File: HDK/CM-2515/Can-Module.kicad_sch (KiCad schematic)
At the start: 13 parts, among them J101 Can Connect, J102 Can Connect, SW101 SW_DIP_x01, U101 SN65HVD230, U102 MCP2515-xST, Y101 8MHz

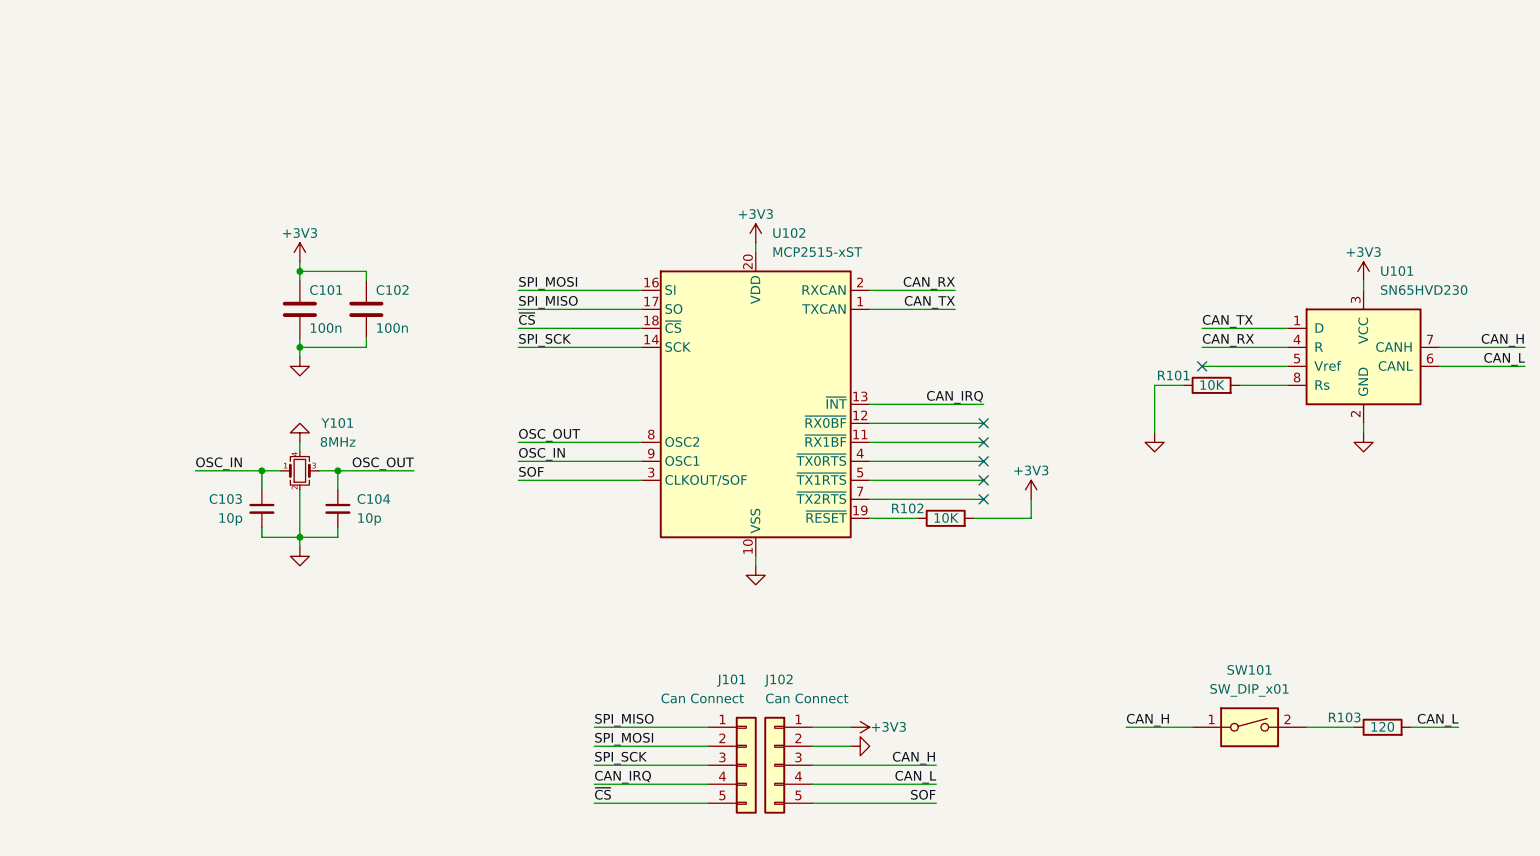
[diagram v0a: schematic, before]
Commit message: updated CM2515
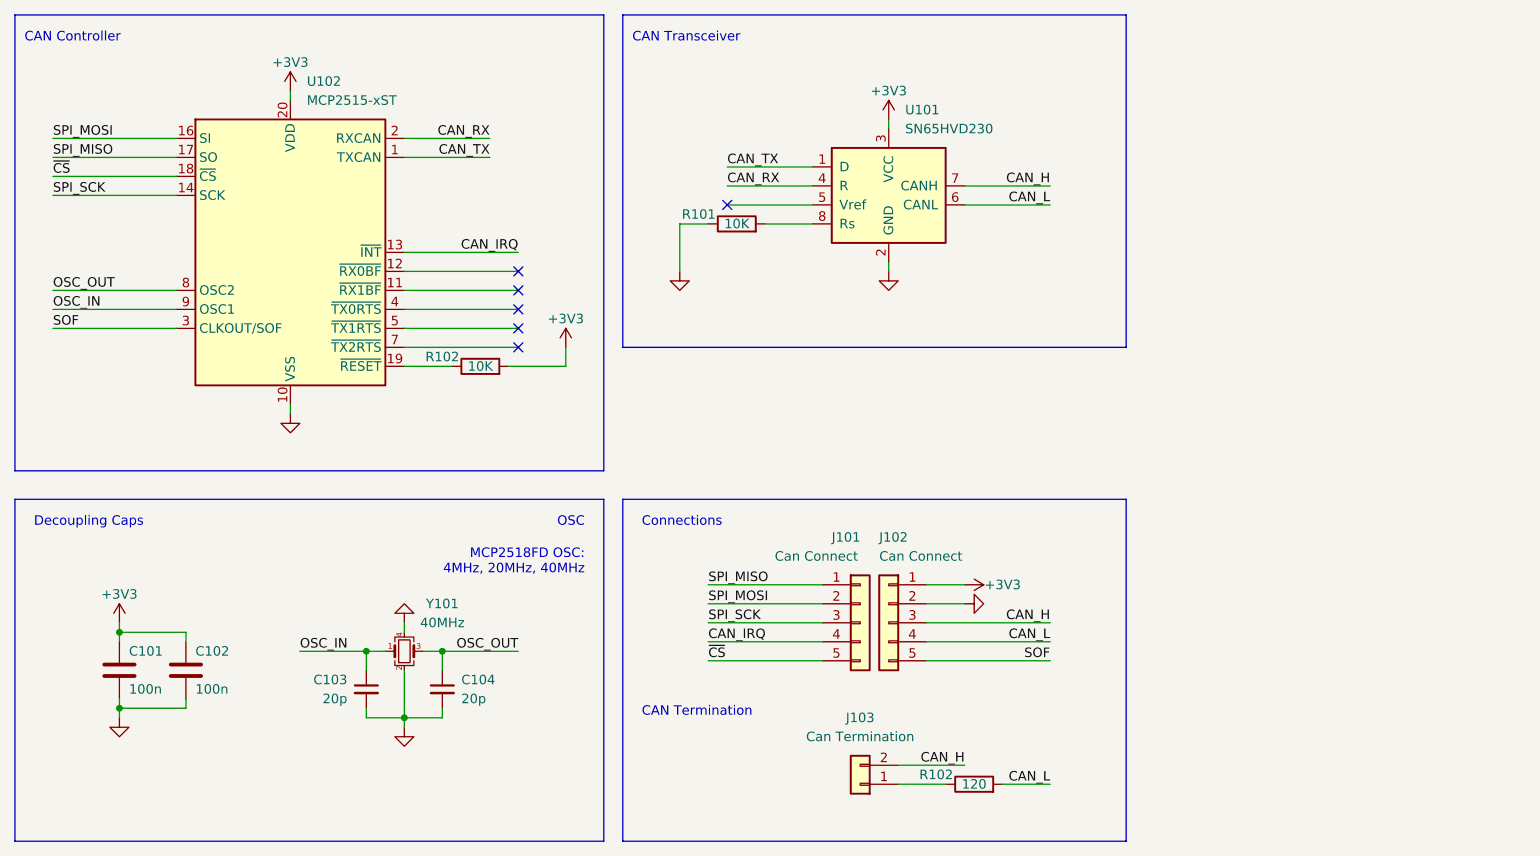
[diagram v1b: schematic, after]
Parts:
- removed R102: 10K, Resistor_SMD:R_0402_1005Metric, symbol Device:R
- removed R103: 120, Resistor_SMD:R_0402_1005Metric, symbol Device:R
- removed SW101: SW_DIP_x01, Button_Switch_SMD:SW_DIP_SPSTx01_Slide_9.78x4.72mm_W8.61mm_P2.54mm, symbol Switch:SW_DIP_x01
- added J103: Can Termination, NVF-Kicad:PinHeader_1x02_P2.54mm_Horizontal, symbol Connector_Generic:Conn_01x02
- added R102: 120, Resistor_SMD:R_0805_2012Metric, symbol Device:R
- added R102: 10K, Resistor_SMD:R_0402_1005Metric, symbol Device:R
- C101, C102: LCSC (none) -> C1523
- C103, C104: value 10p -> 20p; LCSC (none) -> C1554
- R101: LCSC (none) -> C25744
- U101: LCSC (none) -> C12084
- Y101: value 8MHz -> 40MHz; LCSC (none) -> C9010
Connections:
- net +3V3: now also R102.2
- net CAN_H: now also J103.2 (Pin_2)
- net CAN_L: now also R102.2
- net at U102.19 (~{RESET}): now also R102.1
- new net: J103.1 (Pin_1), R102.1
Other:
- note added: "CAN Controller"
- note added: "CAN Termination"
- note added: "CAN Transceiver"
- note added: "Connections"
- note added: "Decoupling Caps"
- note added: "MCP2518FD OSC: 4MHz, 20MHz, 40MHz"
- note added: "OSC"
